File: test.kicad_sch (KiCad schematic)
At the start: 16 parts, among them K3 Relay_DPDT, SW13 SW_LEFT, SW14 SW_RIGHT, SW3 E-STOP, SW5 PROXIMITY_SENSOR, SW7 MODE SWITCH, U7 HS-40005, U8 PID_CONTROL

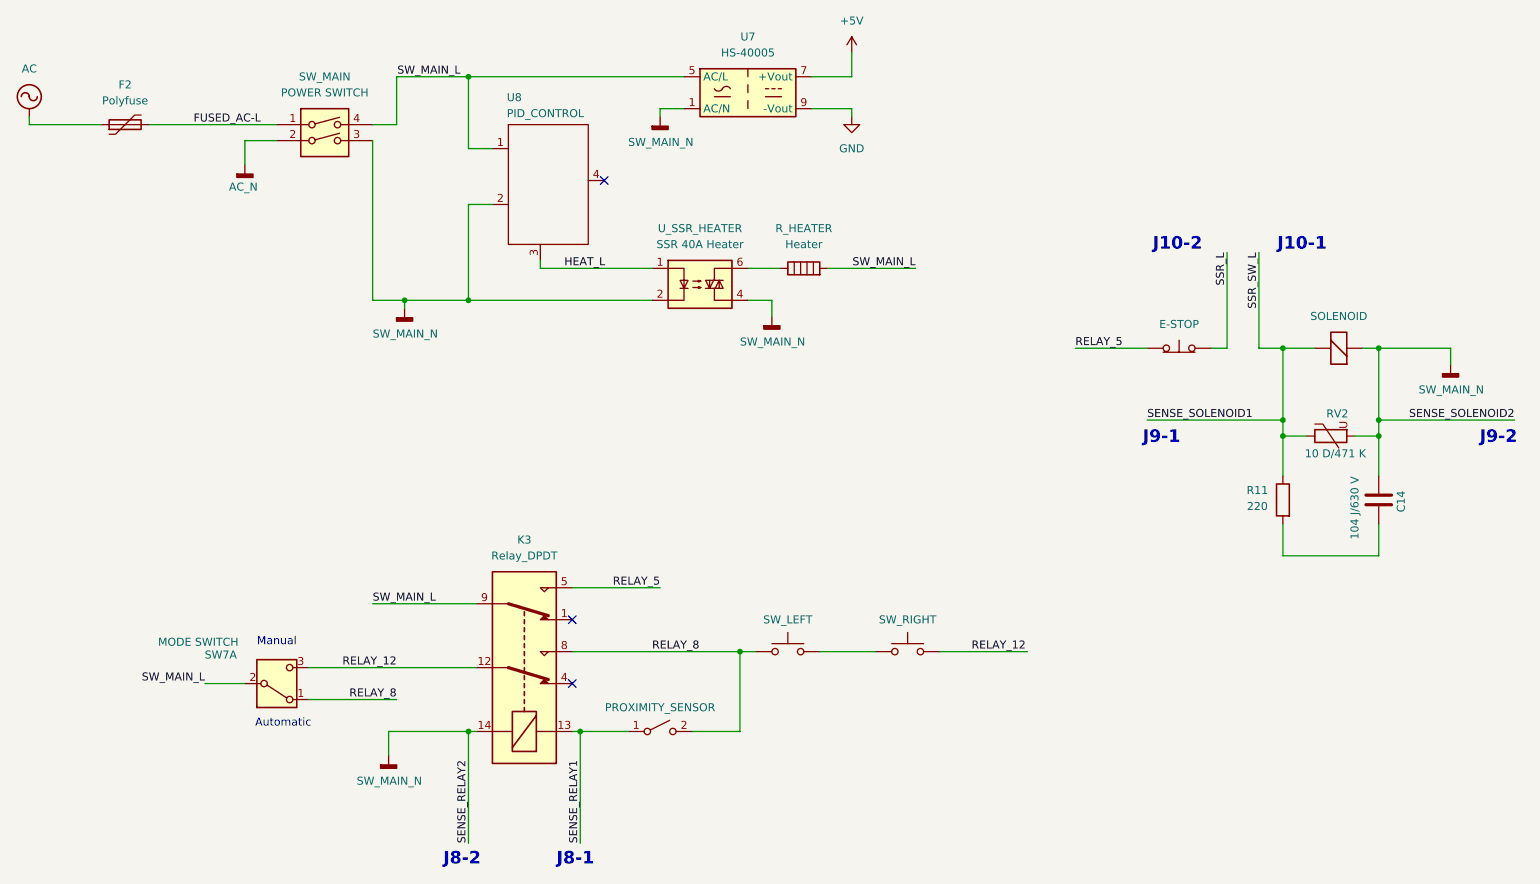
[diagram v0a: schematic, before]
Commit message: add: connector heating SSR
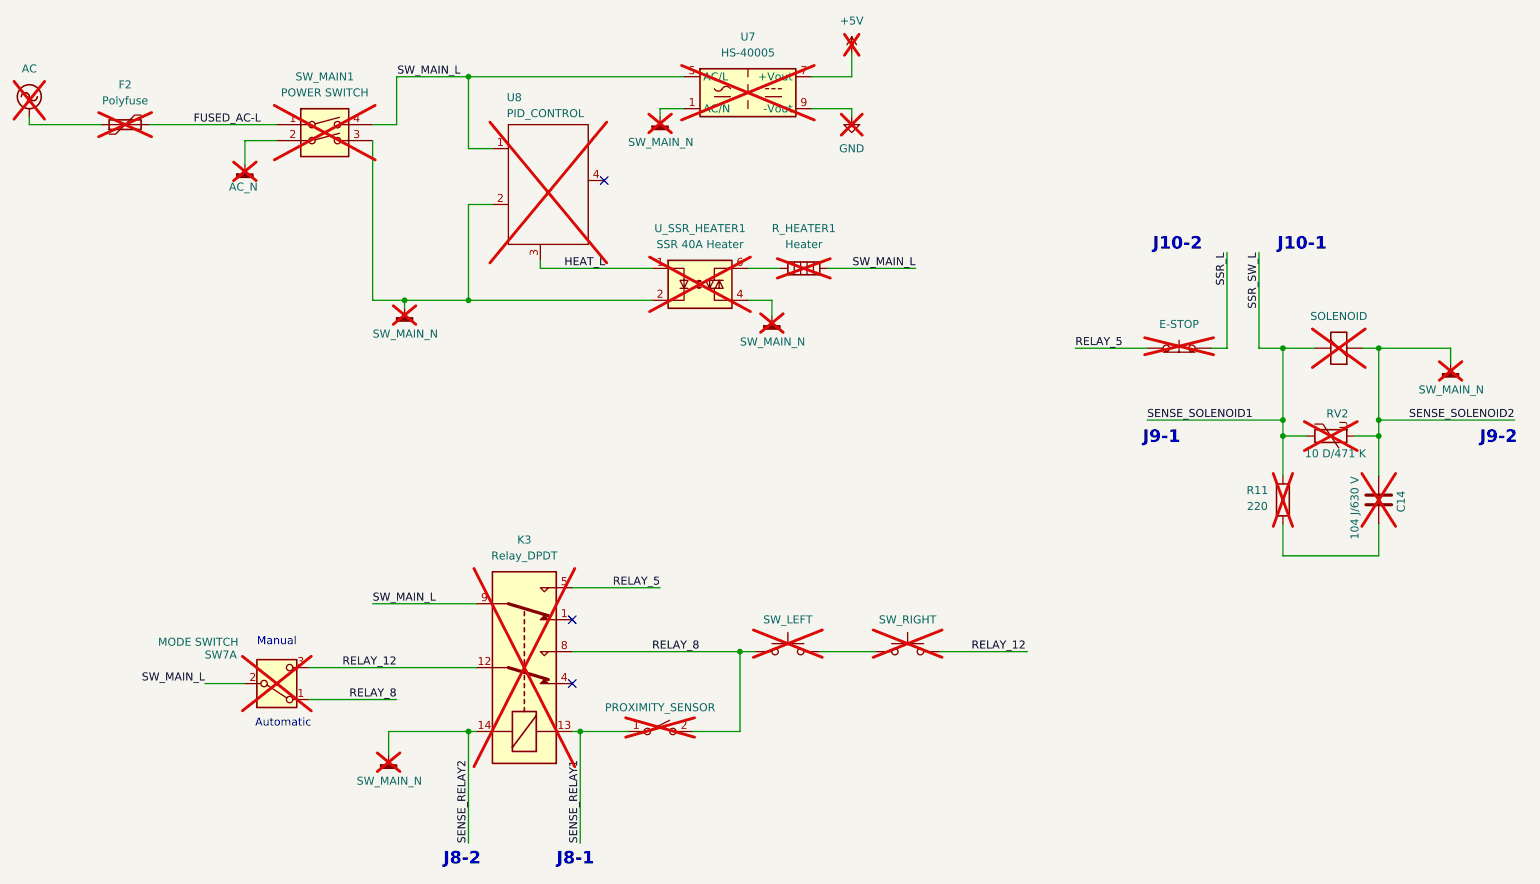
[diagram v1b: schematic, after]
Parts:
- C14, F2, K3, L2, R11, RV2, SW13, SW14, SW3, SW5, SW7, U7, U8: now not fitted; now left out of the parts list
- R_HEATER1: renamed from R_HEATER; now not fitted; now left out of the parts list
- SW_MAIN1: renamed from SW_MAIN; now not fitted; now left out of the parts list
- U_SSR_HEATER1: renamed from U_SSR_HEATER; now not fitted; now left out of the parts list
